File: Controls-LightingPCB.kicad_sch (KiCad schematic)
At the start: 77 parts, among them J1 MinionConn, J2 12VPWRCONN, SW5 TURN_SIGNAL_SW

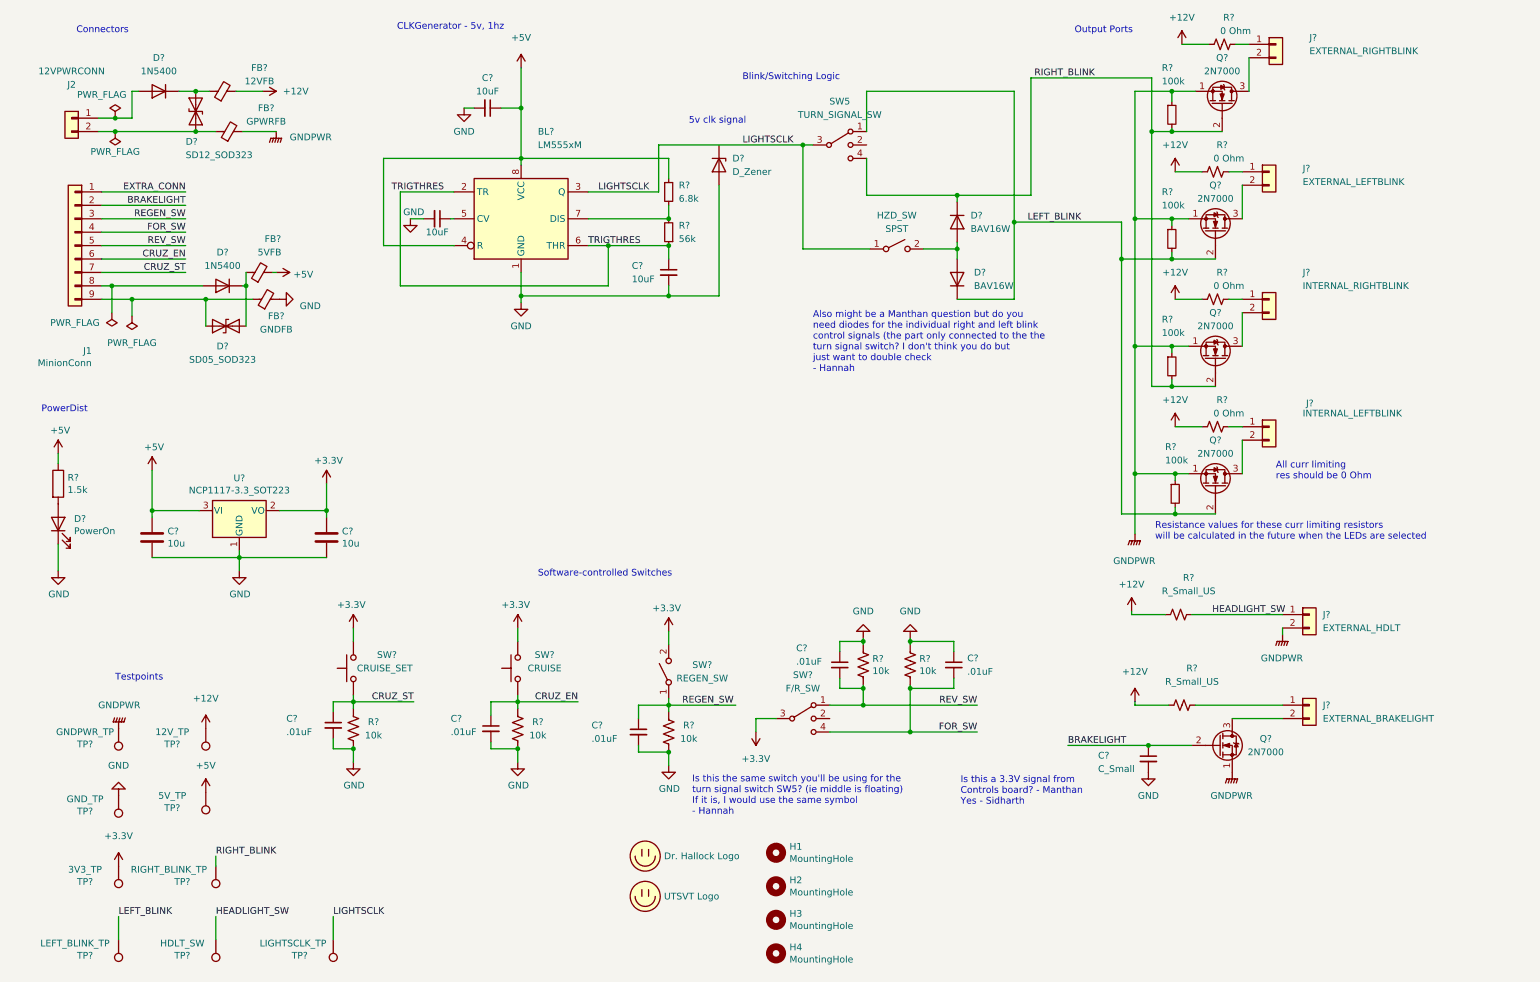
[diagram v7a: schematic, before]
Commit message: finished adding backup ports for gear selector and SW lights
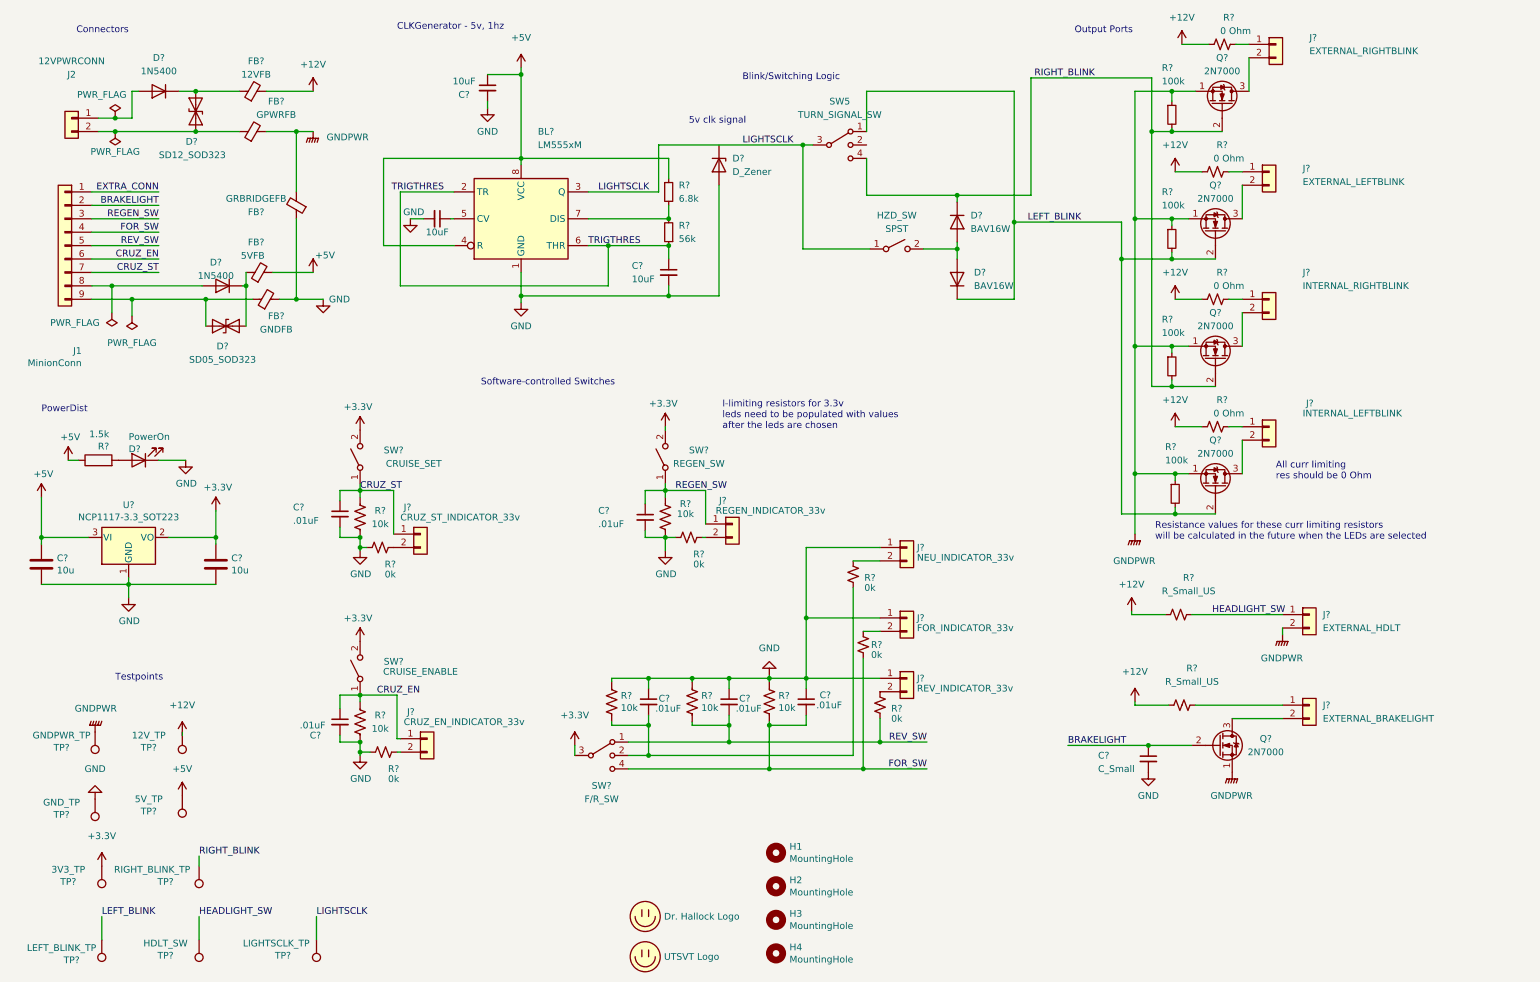
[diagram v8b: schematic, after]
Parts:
- removed SW?: CRUISE, Connector_Molex:Molex_Micro-Fit_3.0_43650-0200_1x02_P3.00mm_Horizontal, symbol Switch:SW_Push
- removed SW?: CRUISE_SET, Connector_Molex:Molex_Micro-Fit_3.0_43650-0200_1x02_P3.00mm_Horizontal, symbol Switch:SW_Push
- added C?: .01uF, symbol Device:C_Small
- added FB?: GRBRIDGEFB, symbol Device:FerriteBead_Small
- added J?: FOR_INDICATOR_33v, Connector_Molex:Molex_Micro-Fit_3.0_43650-0200_1x02_P3.00mm_Horizontal, symbol Connector_Generic:Conn_01x02
- added J?: NEU_INDICATOR_33v, Connector_Molex:Molex_Micro-Fit_3.0_43650-0200_1x02_P3.00mm_Horizontal, symbol Connector_Generic:Conn_01x02
- added J?: CRUZ_EN_INDICATOR_33v, Connector_Molex:Molex_Micro-Fit_3.0_43650-0200_1x02_P3.00mm_Horizontal, symbol Connector_Generic:Conn_01x02
- added J?: REV_INDICATOR_33v, Connector_Molex:Molex_Micro-Fit_3.0_43650-0200_1x02_P3.00mm_Horizontal, symbol Connector_Generic:Conn_01x02
- added J?: CRUZ_ST_INDICATOR_33v, Connector_Molex:Molex_Micro-Fit_3.0_43650-0200_1x02_P3.00mm_Horizontal, symbol Connector_Generic:Conn_01x02
- added J?: REGEN_INDICATOR_33v, Connector_Molex:Molex_Micro-Fit_3.0_43650-0200_1x02_P3.00mm_Horizontal, symbol Connector_Generic:Conn_01x02
- added R? (x6): 0k, symbol Device:R_Small_US
- added R?: 10k, Resistor_SMD:R_0805_2012Metric, symbol Device:R_US
- added SW?: CRUISE_ENABLE, Connector_Molex:Molex_Micro-Fit_3.0_43650-0200_1x02_P3.00mm_Horizontal, symbol Switch:SW_SPST
- added SW?: CRUISE_SET, Connector_Molex:Molex_Micro-Fit_3.0_43650-0200_1x02_P3.00mm_Horizontal, symbol Switch:SW_SPST
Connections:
- net +3V3: now also SW?.2 (B), SW?.2 (B)
- net CRUZ_EN: now also J?.1 (Pin_1), SW?.1 (A)
- net CRUZ_ST: now also J?.1 (Pin_1), SW?.1 (A)
- net FOR_SW: now also R?.2
- net GND: now also C?.1, FB?.1, J?.1 (Pin_1), J?.1 (Pin_1), J?.1 (Pin_1), R?.1, R?.2, R?.2, R?.2
- net GNDPWR: now also FB?.2
- net REGEN_SW: now also J?.1 (Pin_1)
- net REV_SW: now also R?.2
- net at SW?.2: now also C?.2, R?.2, R?.2
- new net: J?.2 (Pin_2), R?.1 (x6)
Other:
- note added: "I-limiting resistors for 3.3v leds need to be populated with values after the leds are chosen"
- note removed: "Also might be a Manthan question but do you need diodes for the individual right and left blink control signals (the part only connected to the the turn signal switch? I don't think you do but just want to double check - Hannah"
- note removed: "Is this a 3.3V signal from Controls board? - Manthan Yes - Sidharth"
- note removed: "Is this the same switch you'll be using for the turn signal switch SW5? (ie middle is floating) If it is, I would use the same symbol - Hannah"
- moved on the sheet: C?, D?, FB?, J1, R?, SW?, TP?, U?
